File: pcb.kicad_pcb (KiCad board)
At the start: 2 copper layers, 21 parts, among them U1 Pico

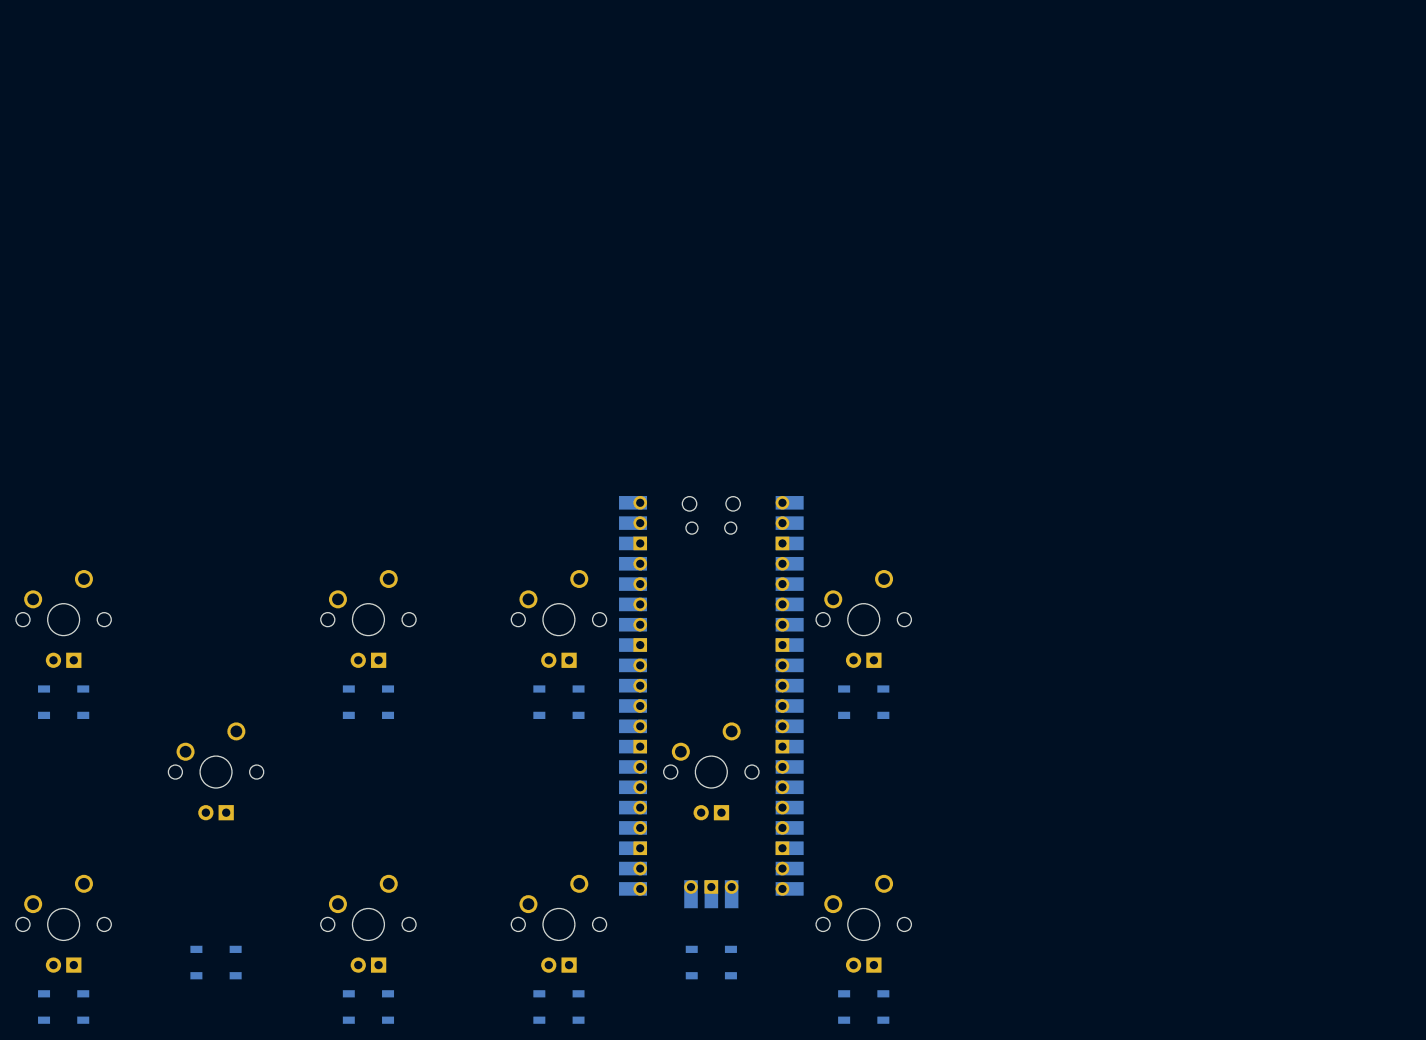
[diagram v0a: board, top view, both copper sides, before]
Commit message: P2 initial routing done
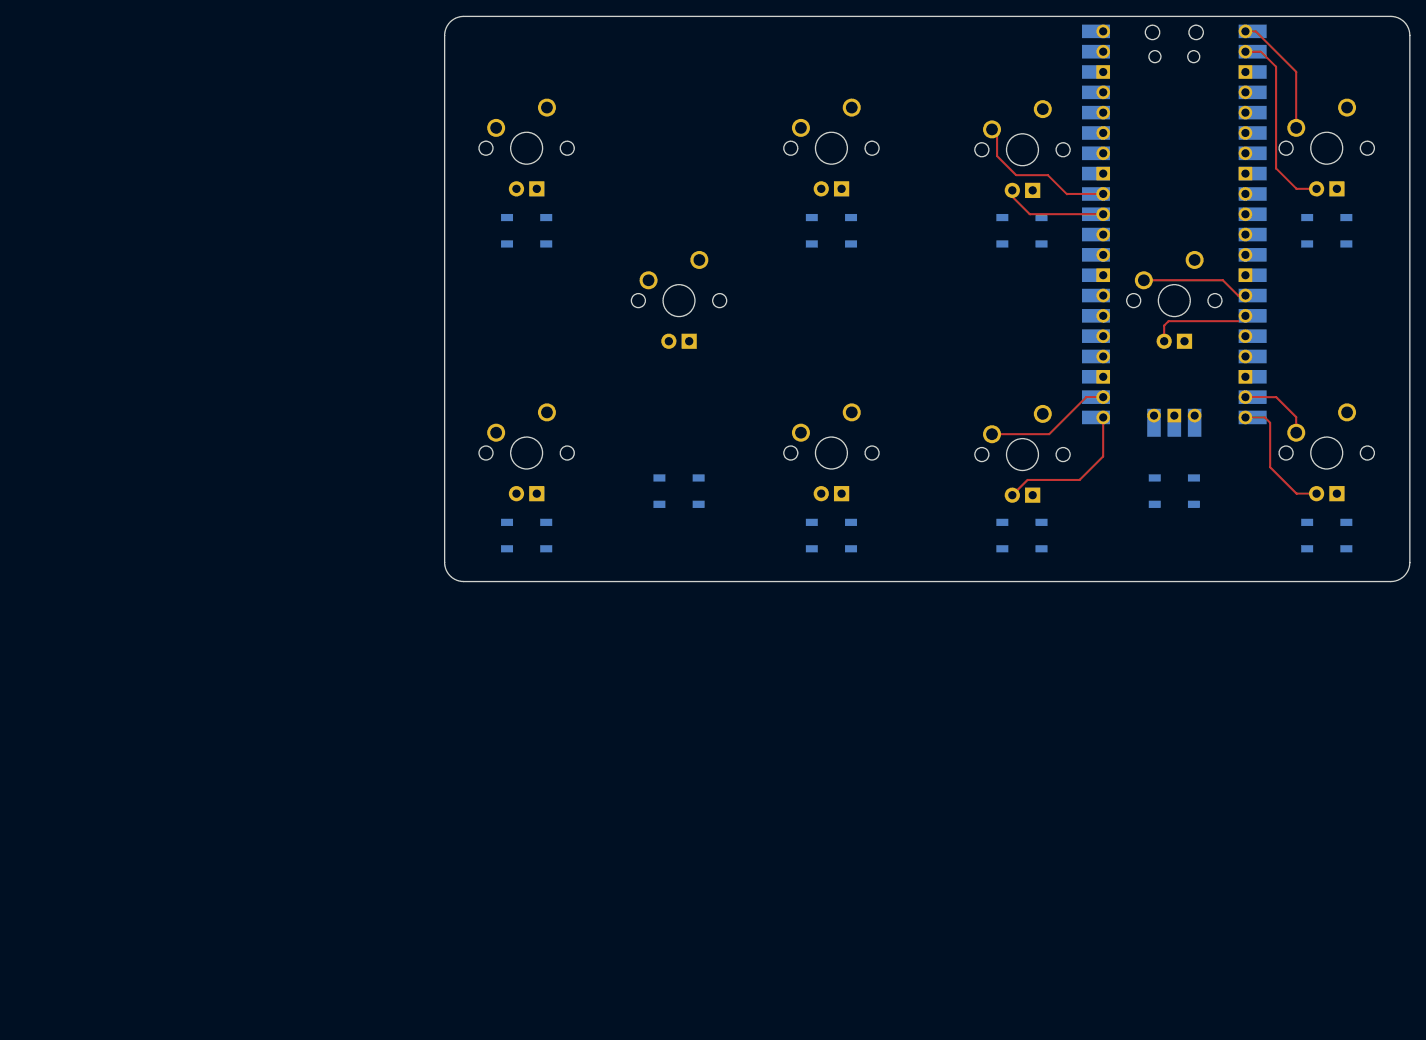
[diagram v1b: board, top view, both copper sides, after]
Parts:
- moved MX6 112.8 mm to (154.0, 76.2)
- moved D4 82.6 mm to (130.1, 86.3)
- moved D7 82.6 mm to (153.9, 86.3)
- moved MX4 82.6 mm to (130.1, 76.0)
- moved MX5 82.6 mm to (130.1, 114.1)
- moved D2 82.6 mm to (92.0, 86.3)
- moved D3 82.6 mm to (111.1, 118.9)
- moved D8 82.6 mm to (173.0, 118.9)
- moved D9 82.6 mm to (192.0, 86.3)
- moved MX1 82.6 mm to (92.0, 114.1)
- moved MX10 82.6 mm to (192.0, 114.1)
- moved MX2 82.6 mm to (92.0, 76.0)
- moved MX3 82.6 mm to (111.1, 95.1)
- moved MX8 82.6 mm to (173.0, 95.1)
- moved MX9 82.6 mm to (192.0, 76.0)
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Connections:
- MX8 pad 1: P2 C -> P2 CN
- U1 pad 1: WS2812B -> P2 UR
- U1 pad 10: P1 UR LED -> unconnected-(U1-Pad10)
- U1 pad 11: P1 CN LED -> unconnected-(U1-Pad11)
- U1 pad 12: P1 UL LED -> unconnected-(U1-Pad12)
- U1 pad 14: P1 DL LED -> P2 CN
- U1 pad 15: P1 DR -> P2 CN LED
- U1 pad 16: P1 UR -> unconnected-(U1-Pad16)
- U1 pad 17: P1 CN -> unconnected-(U1-Pad17)
- U1 pad 19: P1 UL -> P2 DR
- U1 pad 2: P2 DR LED -> P2 UR LED
- U1 pad 20: P1 DL -> P2 DR LED
- U1 pad 21: P2 DL -> P2 DL LED
- U1 pad 22: P2 UL -> P2 DL
- U1 pad 24: P2 CN -> unconnected-(U1-Pad24)
- U1 pad 25: P2 UR -> unconnected-(U1-Pad25)
- U1 pad 26: P2 DR -> unconnected-(U1-Pad26)
- U1 pad 31: unconnected-(U1-Pad31) -> P2 UL LED
- U1 pad 32: unconnected-(U1-Pad32) -> P2 UL
- U1 pad 4: P2 UR LED -> unconnected-(U1-Pad4)
- U1 pad 5: P2 CN LED -> unconnected-(U1-Pad5)
- U1 pad 6: P2 UL LED -> unconnected-(U1-Pad6)
- U1 pad 7: P2 DL LED -> unconnected-(U1-Pad7)
- U1 pad 9: P1 DR LED -> unconnected-(U1-Pad9)
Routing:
- net P2 UR LED: track 0.00 -> 23.4 mm
- net P2 UL: track 0.00 -> 18.8 mm
- net P2 DL LED: track 0.00 -> 18.2 mm
- net P2 UR: track 0.00 -> 17.1 mm
- net P2 DR LED: track 0.00 -> 16.1 mm
- net P2 DL: track 0.00 -> 15.8 mm
- net P2 CN: track 0.00 -> 13.5 mm
- net P2 UL LED: track 0.00 -> 13.1 mm
- net P2 CN LED: track 0.00 -> 11.5 mm
- net P2 DR: track 0.00 -> 9.33 mm
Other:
- board outline added: 120.7 x 70.6 mm

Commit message: Update P2 routing (this is hard D:)
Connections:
- U1 pad 14: P2 CN -> unconnected-(U1-Pad14)
- U1 pad 15: P2 CN LED -> unconnected-(U1-Pad15)
- U1 pad 19: P2 DR -> unconnected-(U1-Pad19)
- U1 pad 20: P2 DR LED -> unconnected-(U1-Pad20)
- U1 pad 4: unconnected-(U1-Pad4) -> P2 CN
- U1 pad 5: unconnected-(U1-Pad5) -> P2 CN LED
- U1 pad 6: unconnected-(U1-Pad6) -> P2 DR
- U1 pad 7: unconnected-(U1-Pad7) -> P2 DR LED
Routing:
- net P2 DR: track 9.33 -> 41.1 mm
- net P2 DR LED: track 16.1 -> 47.7 mm
- net P2 CN LED: track 11.5 -> 36.5 mm
- net P2 CN: track 13.5 -> 28.8 mm
- net P2 UR LED: track 23.4 -> 22.5 mm
- net unconnected-(U1-Pad14): track 0.00 -> 0.92 mm

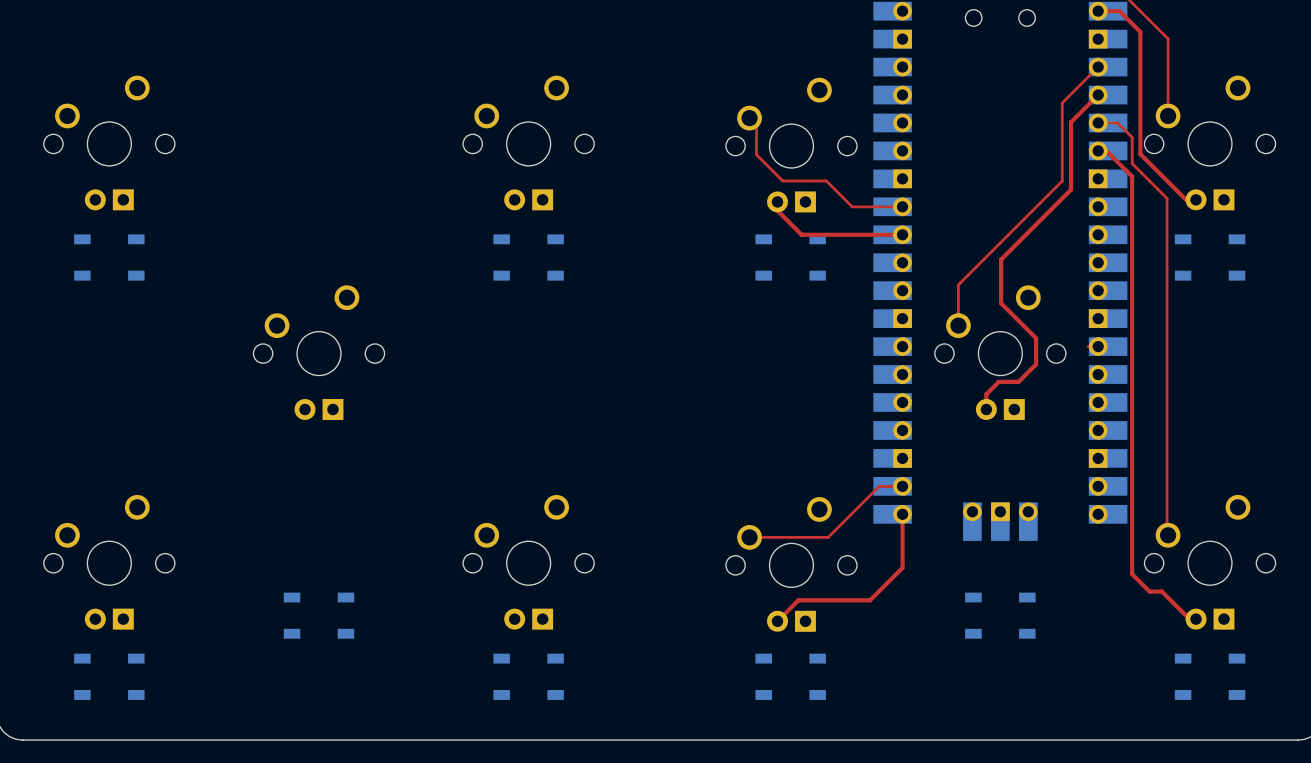
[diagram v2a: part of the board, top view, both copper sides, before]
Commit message: P1 initial routing, no more WS2812Bs built in
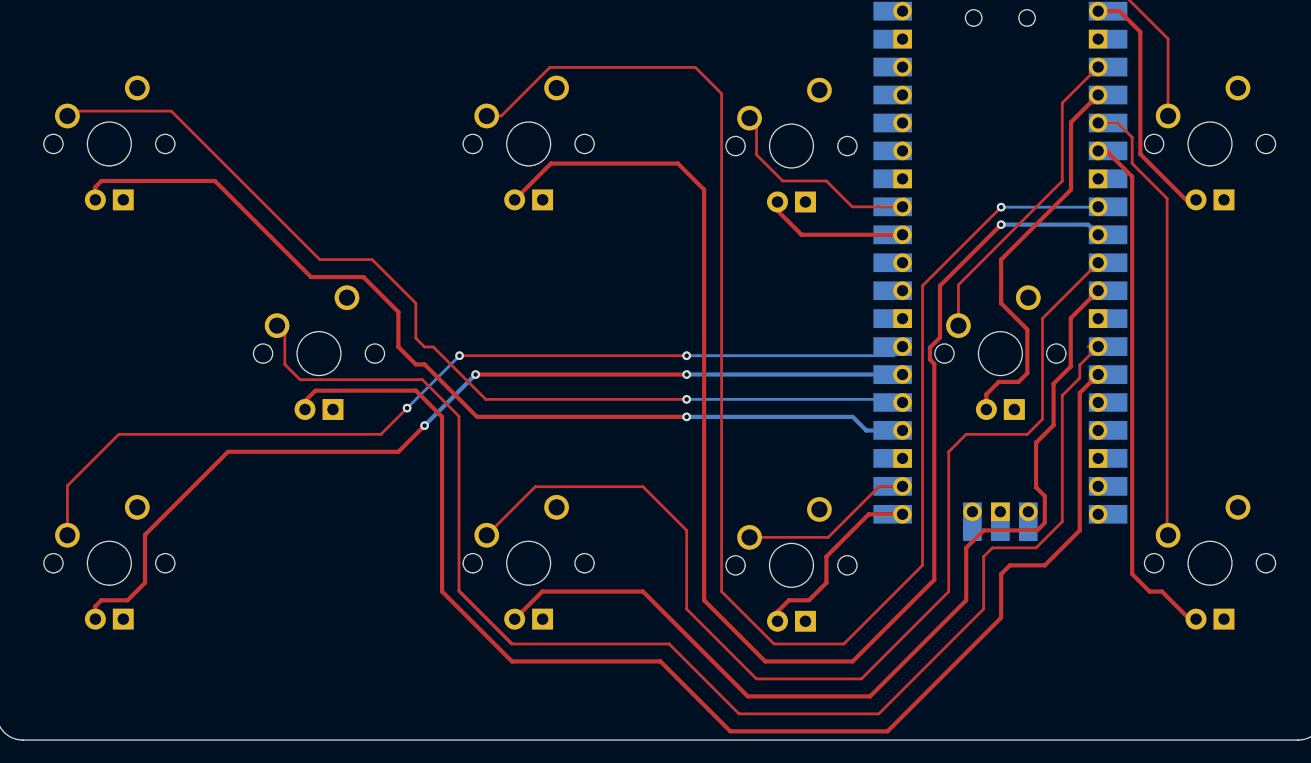
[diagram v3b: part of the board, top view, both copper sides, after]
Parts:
- removed D1, D10, D2, D3, D4, D5, D6, D7, D8, D9: WS2812B, LED_SMD:LED_WS2812B_PLCC4_5.0x5.0mm_P3.2mm
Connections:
- MX3 pad 1: P1 C -> P1 CN
- U1 pad 10: unconnected-(U1-Pad10) -> P1 UR LED
- U1 pad 11: unconnected-(U1-Pad11) -> P1 DR
- U1 pad 12: unconnected-(U1-Pad12) -> P1 DR LED
- U1 pad 14: unconnected-(U1-Pad14) -> P1 CN
- U1 pad 15: unconnected-(U1-Pad15) -> P1 CN LED
- U1 pad 24: unconnected-(U1-Pad24) -> P1 DL LED
- U1 pad 25: unconnected-(U1-Pad25) -> P1 DL
- U1 pad 26: unconnected-(U1-Pad26) -> P1 UL LED
- U1 pad 27: unconnected-(U1-Pad27) -> P1 UL
- U1 pad 9: unconnected-(U1-Pad9) -> P1 UR
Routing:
- net P1 UR: track 0.00 -> 136.9 mm, vias 0 -> 1
- net P1 CN: track 0.00 -> 131.9 mm
- net P1 UR LED: track 0.00 -> 127.5 mm, vias 0 -> 1
- net P1 CN LED: track 0.00 -> 118.4 mm
- net P1 DR: track 0.00 -> 97.3 mm
- net P1 DL: track 0.00 -> 88.9 mm, vias 0 -> 1
- net P1 DR LED: track 0.00 -> 86.2 mm
- net P1 DL LED: track 0.00 -> 86.0 mm, vias 0 -> 1
- net P1 UL LED: track 0.00 -> 85.8 mm, vias 0 -> 3
- net P1 UL: track 0.00 -> 85.6 mm, vias 0 -> 3
- net P2 DL LED: track 18.2 -> 17.3 mm
- net unconnected-(U1-Pad14): track 0.92 -> 0.00 mm
- net P2 CN LED: track 36.5 -> 35.8 mm
